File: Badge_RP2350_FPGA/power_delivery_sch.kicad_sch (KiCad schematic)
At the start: 23 parts, among them U3 ME6211C12, U4 TMI7003C

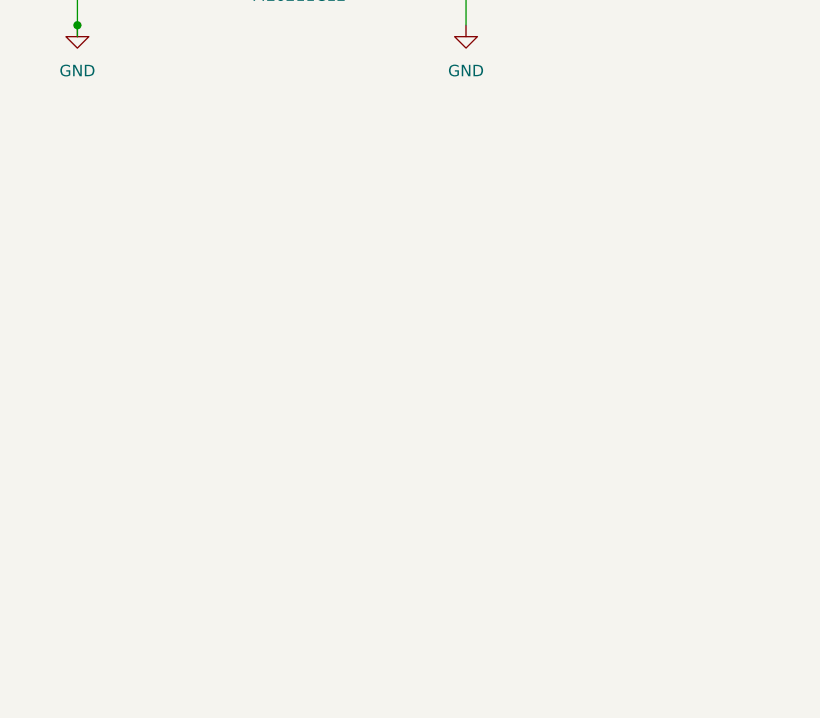
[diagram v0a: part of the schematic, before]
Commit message: add type c port and uart connections
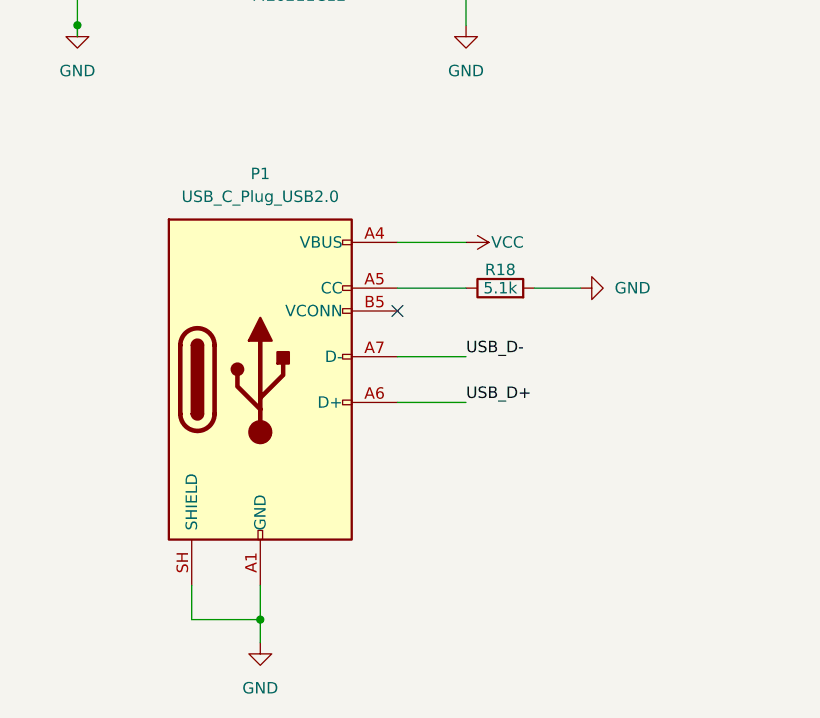
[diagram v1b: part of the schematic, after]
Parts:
- added P1: USB_C_Plug_USB2.0, Connector_USB:USB_C_Receptacle_HRO_TYPE-C-31-M-12, symbol Connector:USB_C_Plug_USB2.0
- added R18: 5.1k, Resistor_THT:R_Axial_DIN0204_L3.6mm_D1.6mm_P1.90mm_Vertical, symbol Device:R
- C1, C2, C5: footprint Capacitor_SMD:CP_Elec_3x5.3 -> Capacitor_SMD:C_0402_1005Metric
- U3: footprint mylibraryprint:ME6211C12 -> semitovpartslibrary:ME6211C12
- U4: footprint mylibraryprint:TMI7003C -> semitovpartslibrary:TMI7003C
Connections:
- net GND: now also P1.A1 (GND), P1.A12 (GND), P1.B1 (GND), P1.B12 (GND), P1.SH (SHIELD), R18.2
- net VCC: now also P1.A4 (VBUS), P1.A9 (VBUS), P1.B4 (VBUS), P1.B9 (VBUS)
- new net: P1.A5 (CC), R18.1
- new net USB_D+: P1.A6 (D+)
- new net USB_D-: P1.A7 (D-)
- no-connect marks 1 -> 2
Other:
- company: (none) -> SemiTO-V, RISC-V Student Team
- title: (none) -> RISC-V Summit Europe Badge

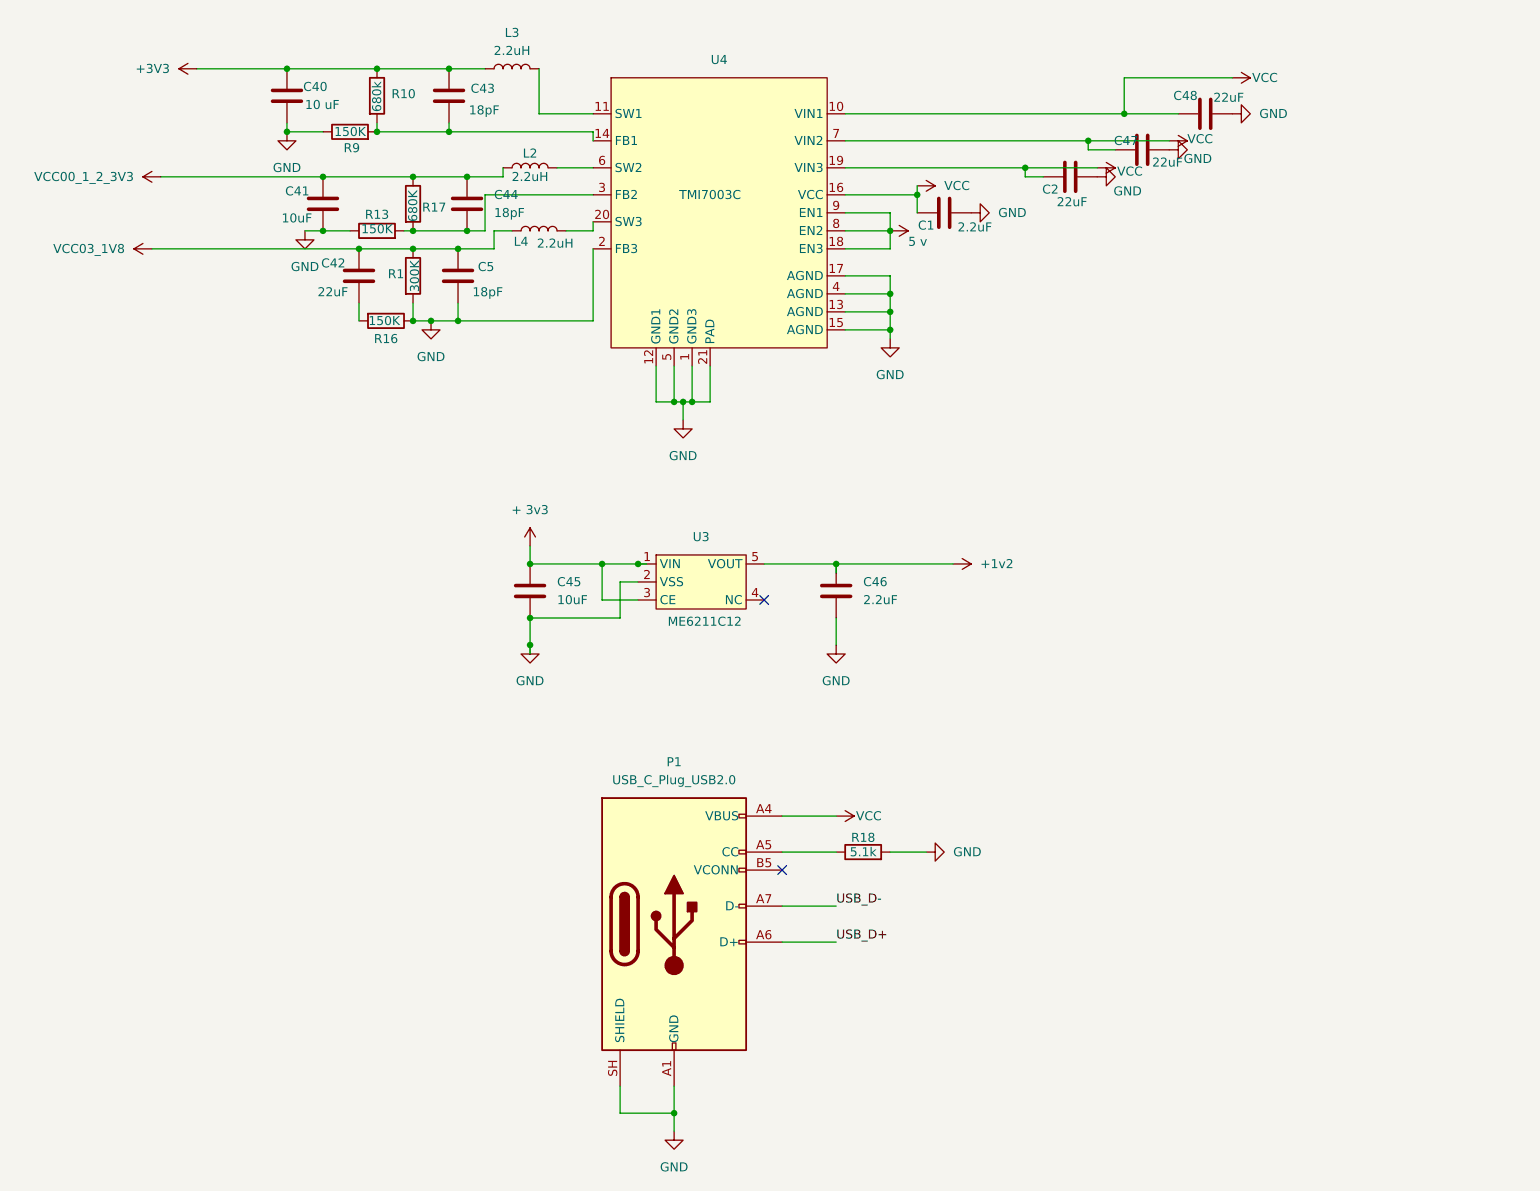
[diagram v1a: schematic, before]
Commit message: modify usb and flash connections
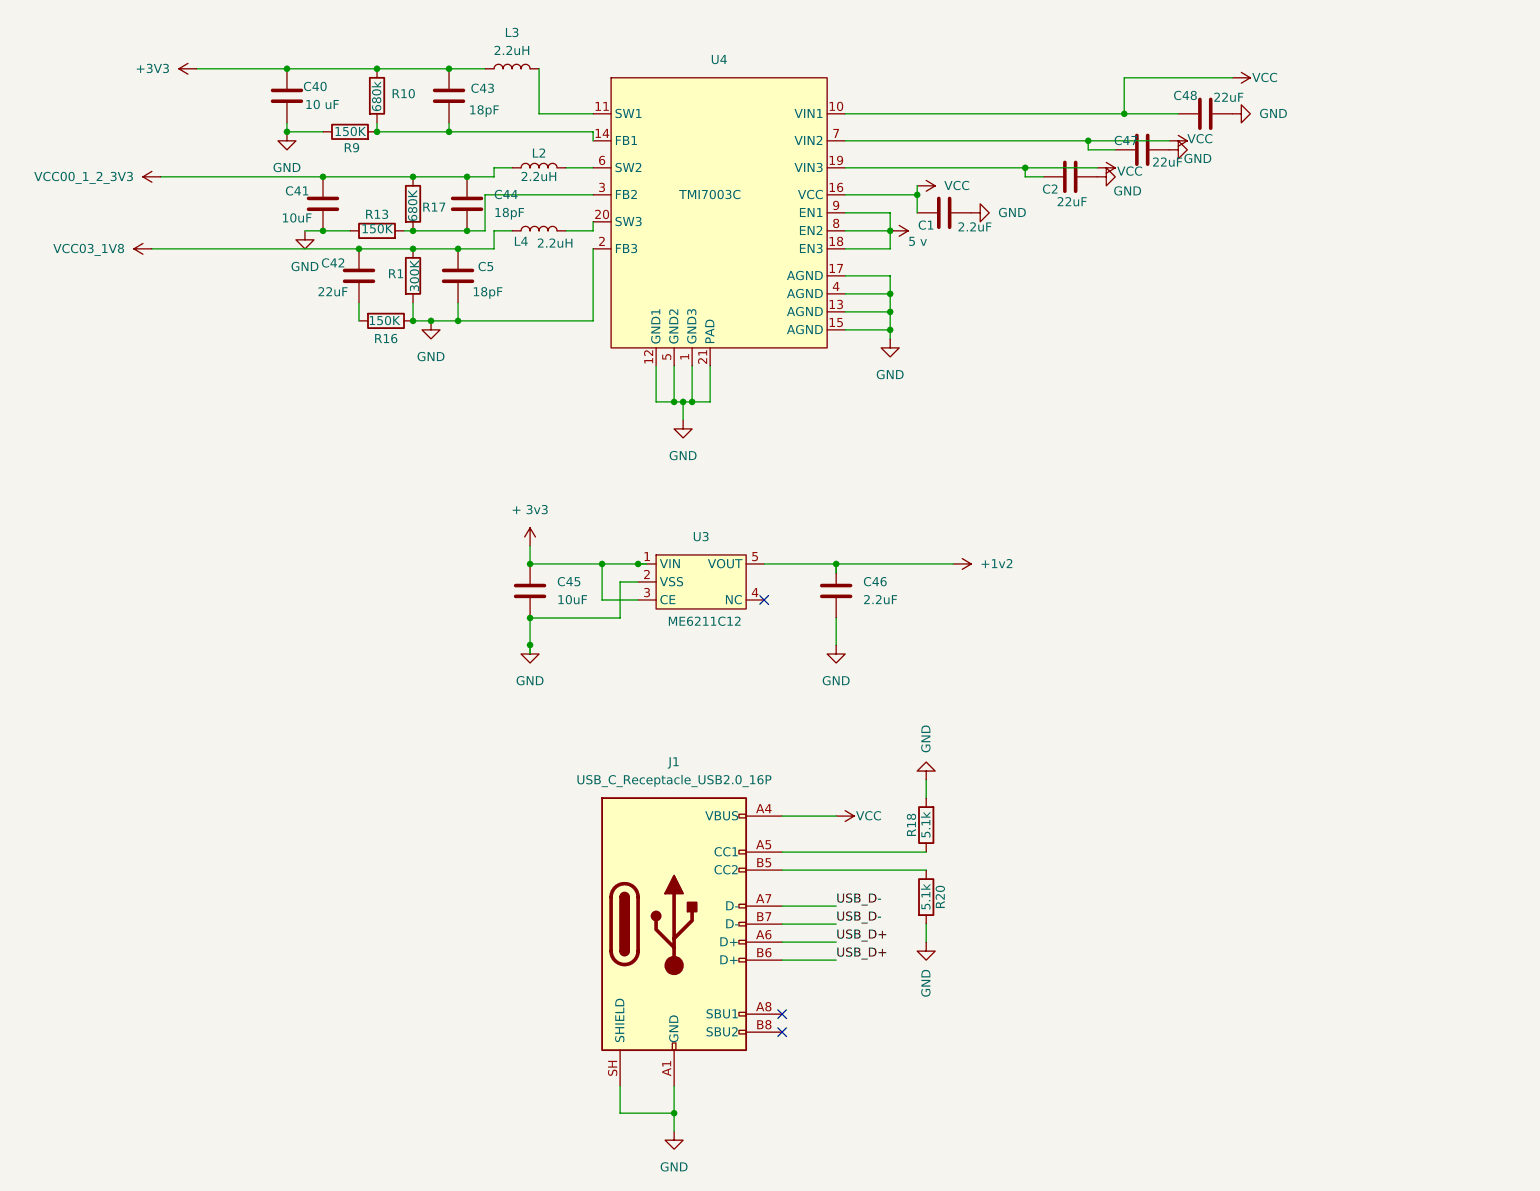
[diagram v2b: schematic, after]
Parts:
- removed P1: USB_C_Plug_USB2.0, Connector_USB:USB_C_Receptacle_HRO_TYPE-C-31-M-12, symbol Connector:USB_C_Plug_USB2.0
- added J1: USB_C_Receptacle_USB2.0_16P, symbol Connector:USB_C_Receptacle_USB2.0_16P
- added R20: 5.1k, Resistor_THT:R_Axial_DIN0204_L3.6mm_D1.6mm_P1.90mm_Vertical, symbol Device:R
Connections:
- net GND: now also J1.A1 (GND), J1.A12 (GND), J1.B1 (GND), J1.B12 (GND), J1.SH (SHIELD), R20.2
- net USB_D+: now also J1.A6 (D+), J1.B6 (D+)
- net USB_D-: now also J1.A7 (D-), J1.B7 (D-)
- net VCC: now also J1.A4 (VBUS), J1.A9 (VBUS), J1.B4 (VBUS), J1.B9 (VBUS)
- net at R18.1: now also J1.A5 (CC1)
- new net: J1.B5 (CC2), R20.1
- no-connect marks 2 -> 3
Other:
- moved on the sheet: L2, R18

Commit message: edit schematics, add global pins
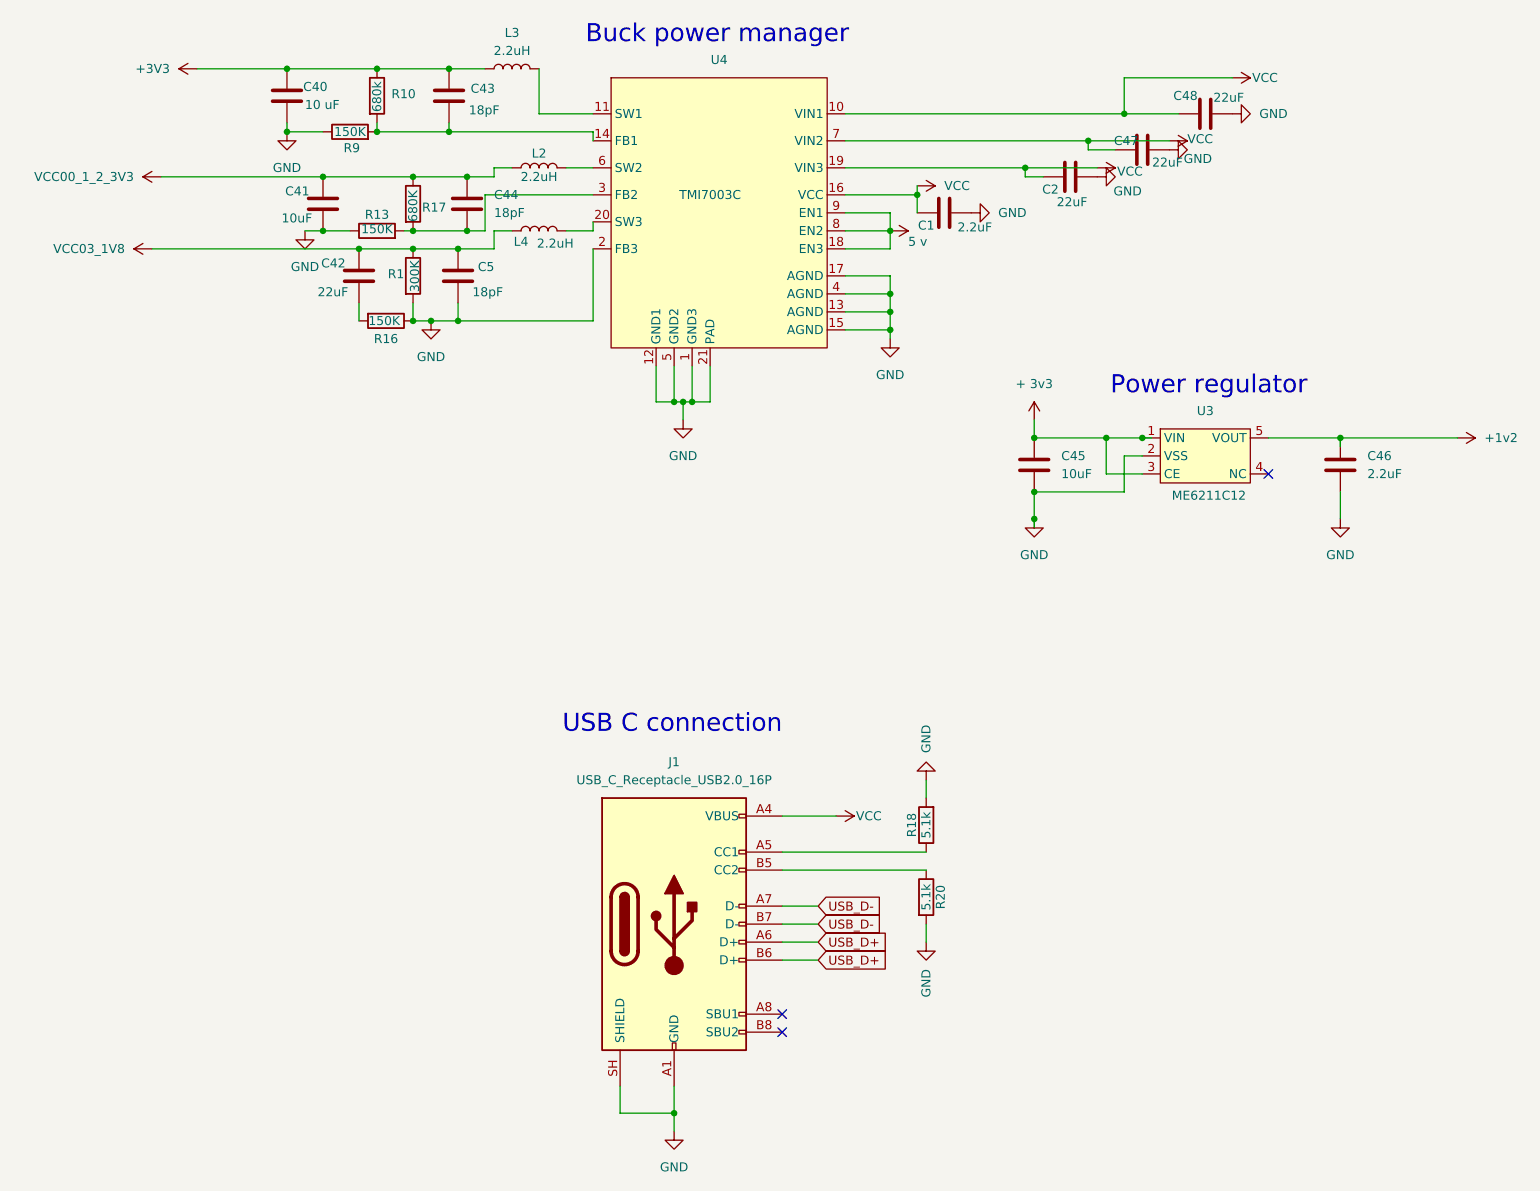
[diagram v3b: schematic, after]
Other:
- note added: "Buck power manager"
- note added: "Power regulator"
- note added: "USB C connection"
- moved on the sheet: C45, C46, U3

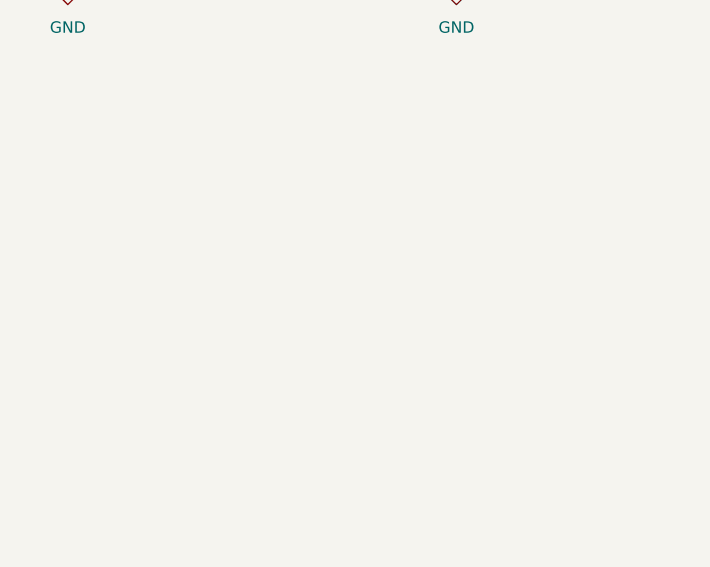
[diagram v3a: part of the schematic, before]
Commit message: assign all footprints and import to pcb
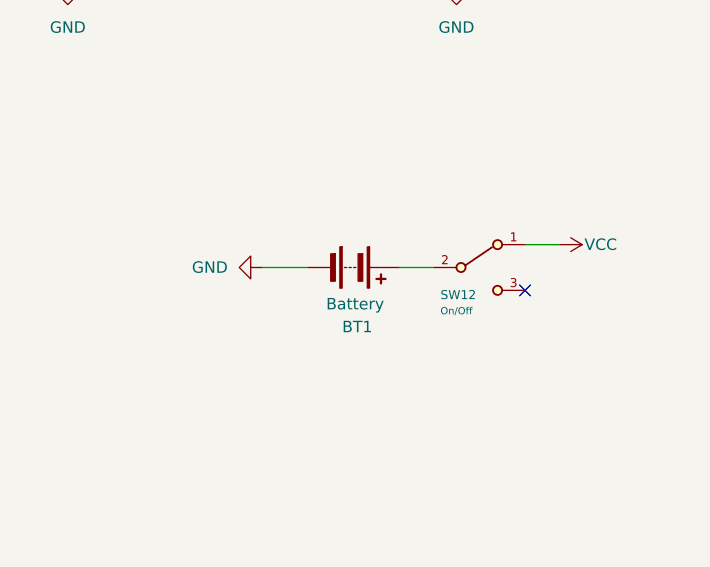
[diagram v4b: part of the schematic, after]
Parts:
- added BT1: Battery, Battery:BatteryHolder_Keystone_2462_2xAA, symbol Device:Battery
- added SW12: On/Off, Button_Switch_SMD:SW_SPDT_CK_JS102011SAQN, symbol HDLib_Switch:SlideSwitch
- C40, C41, C42, C43, C44, C45, C46, C47, C48: footprint Capacitor_SMD:CP_Elec_3x5.3 -> Capacitor_SMD:C_0402_1005Metric
- J1: footprint (none) -> Connector_USB:USB_C_Receptacle_HRO_TYPE-C-31-M-12
- L2, L3, L4: footprint Inductor_SMD:L_6.3x6.3_H3 -> Inductor_SMD:L_APV_ANR4018
- R1, R10, R13, R16, R17, R18, R20, R9: footprint Resistor_THT:R_Axial_DIN0204_L3.6mm_D1.6mm_P1.90mm_Vertical -> Resistor_SMD:R_0402_1005Metric
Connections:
- net GND: now also BT1.2 (-)
- net VCC: now also SW12.1 (A)
- new net: BT1.1 (+), SW12.2 (B)
- no-connect marks 3 -> 4

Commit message: add headers and fix voltage references
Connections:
- net +3V3 is gone; now on net + 3v3: C40.1, C43.1, L3.1, R10.1
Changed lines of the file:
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@@
 		(title "RISC-V Summit Europe Badge")
 		(date "2026-03-29")
-		(rev "v1.3")
+		(rev "v1.4")
 		(company "SemiTO-V, RISC-V Student Team")
 		(comment 3 "License: CERN-OHL-W-2.0")
-		(comment 4 "Authors: Tan Siret Akıncı, Alessandro Bochino, Carlo Bendelli, Arianna Bruno")
+		(comment 4 "Authors: Tan Siret Akıncı, Alessandro Bochino, Carlo Bendelli, Arianna Bruno, Valerio Donnini")
 	)
 	(text "Power regulator"
@@
 	)
 	(symbol
-		(lib_id "power:VCC")
-		(at 43.18 29.21 90)
-		(unit 1)
-		(body_style 1)
-		(exclude_from_sim no)
-		(in_bom yes)
-		(on_board yes)
-		(in_pos_files yes)
-		(dnp no)
-		(fields_autoplaced yes)
-		(property "Reference" "#PWR038"
-			(at 46.99 29.21 0)
-			(hide yes)
-			(show_name no)
-			(do_not_autoplace no)
-			(effects
-				(font
-					(size 1.27 1.27)
-				)
-			)
-		)
-		(property "Value" "+3V3"
-			(at 39.37 29.2099 90)
-			(show_name no)
-			(do_not_autoplace no)
-			(effects
-				(font
-					(size 1.27 1.27)
-				)
-				(justify left)
-			)
-		)
-		(property "Footprint" ""
-			(at 43.18 29.21 0)
-			(hide yes)
-			(show_name no)
-			(do_not_autoplace no)
-			(effects
-				(font
-					(size 1.27 1.27)
-				)
-			)
-		)
-		(property "Datasheet" ""
-			(at 43.18 29.21 0)
-			(hide yes)
-			(show_name no)
-			(do_not_autoplace no)
-			(effects
-				(font
-					(size 1.27 1.27)
-				)
-			)
-		)
-		(property "Description" "Power symbol creates a global label with name \"VCC\""
-			(at 43.18 29.21 0)
-			(hide yes)
-			(show_name no)
-			(do_not_autoplace no)
-			(effects
-				(font
-					(size 1.27 1.27)
-				)
-			)
-		)
-		(pin "1"
-		)
-		(instances
-			(project "Badge_RP2350_FPGA"
-				(path "/0ce87b49-0553-4a87-87c1-84e31180901e/d42deb57-951c-4ebe-afa1-91d9e0ce4651"
-					(reference "#PWR038")
-					(unit 1)
-				)
-			)
-		)
-	)
-	(symbol
 		(lib_id "Device:R")
 		(at 73.66 48.26 0)
@@
 					(unit 1)
 				)
+			)
+		)
+	)
+	(symbol
+		(lib_id "power:VCC")
+		(at 43.18 29.21 90)
+		(unit 1)
+		(body_style 1)
+		(exclude_from_sim no)
+		(in_bom yes)
+		(on_board yes)
+		(in_pos_files yes)
+		(dnp no)
+		(fields_autoplaced yes)
+		(property "Reference" "#PWR071"
+			(at 46.99 29.21 0)
+			(hide yes)
+			(show_name no)
+			(do_not_autoplace no)
+			(effects
+				(font
+					(size 1.27 1.27)
+				)
+			)
+		)
+		(property "Value" "+ 3v3"
+			(at 39.37 29.2099 90)
+			(show_name no)
+			(do_not_autoplace no)
+			(effects
+				(font
+					(size 1.27 1.27)
+				)
+				(justify left)
+			)
+		)
+		(property "Footprint" ""
+			(at 43.18 29.21 0)
+			(hide yes)
+			(show_name no)
+			(do_not_autoplace no)
+			(effects
+				(font
+					(size 1.27 1.27)
+				)
+			)
+		)
+		(property "Datasheet" ""
+			(at 43.18 29.21 0)
+			(hide yes)
+			(show_name no)
+			(do_not_autoplace no)
+			(effects
+				(font
+					(size 1.27 1.27)
+				)
+			)
+		)
+		(property "Description" "Power symbol creates a global label with name \"VCC\""
+			(at 43.18 29.21 0)
+			(hide yes)
+			(show_name no)
+			(do_not_autoplace no)
+			(effects
+				(font
+					(size 1.27 1.27)
+				)
+			)
+		)
+		(pin "1"
+		)
+		(instances
+			(project "Badge_RP2350_FPGA"
+				(path "/0ce87b49-0553-4a87-87c1-84e31180901e/d42deb57-951c-4ebe-afa1-91d9e0ce4651"
+					(reference "#PWR071")
+					(unit 1)
+				)

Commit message: update footprints, connections, some labels and more
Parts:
- SW12: footprint Button_Switch_SMD:SW_SPDT_CK_JS102011SAQN -> semitovpartslibrary:C&K JS102011SAQN
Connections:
- net + 3v3 renamed +3v3

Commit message: edit schematics visually and edit pcb
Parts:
- U3: footprint semitovpartslibrary:ME6211C12 -> semitovpartslibrary:SOT-23-5_L3.0-W1.7-P0.95-LS2.8-BL
- U4: footprint semitovpartslibrary:TMI7003C -> semitovpartslibrary:QFN-20_L3.0-W3.0-P0.40-BL-EP1.7
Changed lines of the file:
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@@
 			)
 		)
-		(property "Footprint" "semitovpartslibrary:ME6211C12"
+		(property "Footprint" "semitovpartslibrary:SOT-23-5_L3.0-W1.7-P0.95-LS2.8-BL"
 			(at 185.42 83.82 0)
 			(hide yes)
@@
 			)
 		)
-		(property "Footprint" "semitovpartslibrary:TMI7003C"
+		(property "Footprint" "semitovpartslibrary:QFN-20_L3.0-W3.0-P0.40-BL-EP1.7"
 			(at 115.57 46.99 0)
 			(hide yes)
